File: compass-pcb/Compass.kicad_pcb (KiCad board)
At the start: 2 copper layers, 6 parts

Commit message: adding comments to psb
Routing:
- net (no net): track 950.9 -> 913.0 mm, vias 36 -> 38
- net GND: track 142.4 -> 175.8 mm, vias 6 -> 8
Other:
- board text added: "Battery"
- board text added: "Encoder"
- board text added: "GPS"
- board text added: "Hall Sensor (B)"
- board text added: "Power (charge/ discharge)"
- board text added: "Servo (A)"

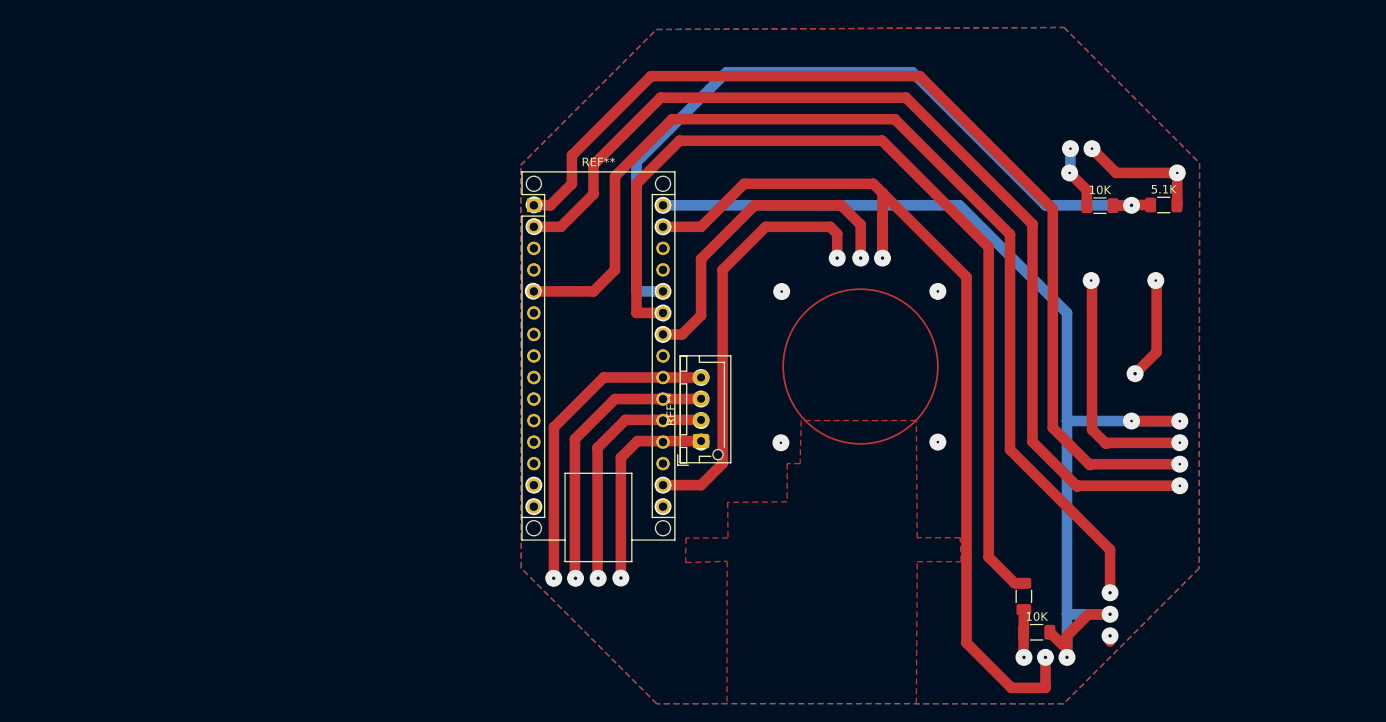
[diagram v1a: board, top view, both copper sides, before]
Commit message: adding battery jumper
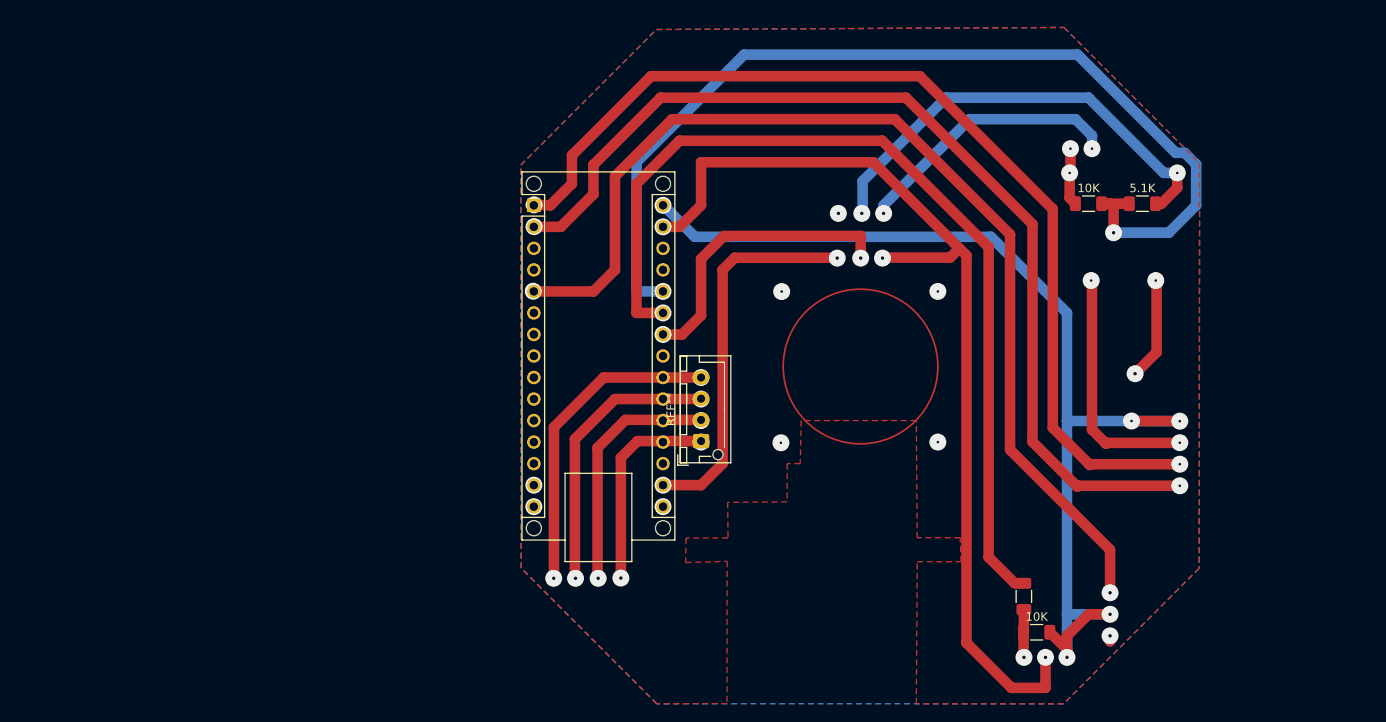
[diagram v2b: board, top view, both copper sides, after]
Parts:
- moved 5.1K 2.52 mm to (240.0, 76.0)
- moved 10K 1.36 mm to (233.7, 76.0)
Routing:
- net (no net): track 913.0 -> 1000.3 mm, vias 38 -> 41
- net GND: track 175.8 -> 179.2 mm
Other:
- board text added: "Battery gnd +"
- board text added: "Battery jumper"
- board text removed: "Battery"

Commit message: playing with placing main switch on the board
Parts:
- added  : , Connector_Wire:SolderWire-0.5sqmm_1x01_D0.9mm_OD2.1mm, F.Cu at (209.5, 82.4)
- added REF**: SolderWire-1.5sqmm_1x01_D1.7mm_OD3.9mm, Connector_Wire:SolderWire-1.5sqmm_1x01_D1.7mm_OD3.9mm, F.Cu at (264.2, 91.4)
- added REF**: SolderWire-2.5sqmm_1x01_D2.4mm_OD3.6mm, Connector_Wire:SolderWire-2.5sqmm_1x01_D2.4mm_OD3.6mm, F.Cu at (264.2, 83.8)
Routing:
- net (no net): track 1000.3 -> 1003.8 mm, vias 41 -> 58
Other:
- board text added: "on/off slide switch"

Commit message: Revert "playing with placing main switch on the board"
This reverts commit f90624a9c38ec8366b61e906c035f362712ec212.
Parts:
- removed  : , Connector_Wire:SolderWire-0.5sqmm_1x01_D0.9mm_OD2.1mm
- removed the REF** at (264.2, 91.4)
- removed the REF** at (264.2, 83.8)
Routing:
- net (no net): track 1003.8 -> 1000.3 mm, vias 58 -> 41
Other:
- board text removed: "on/off slide switch"

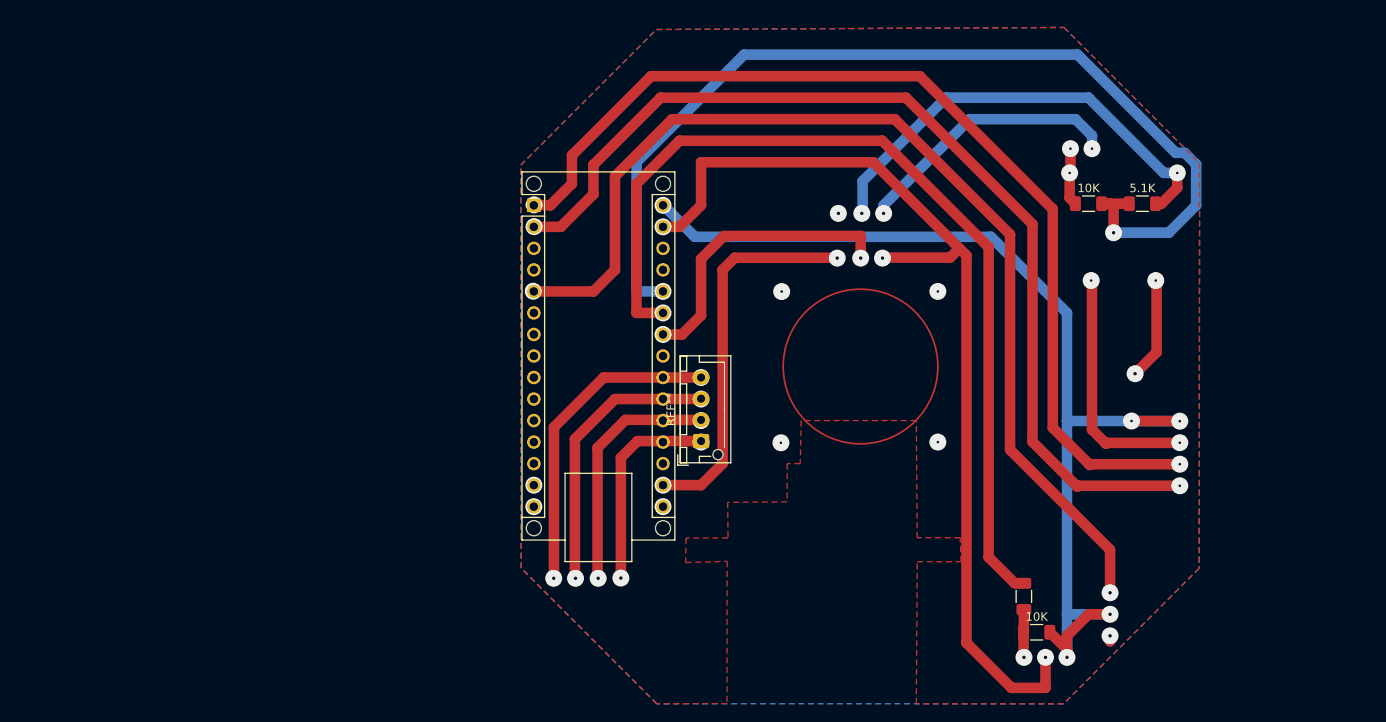
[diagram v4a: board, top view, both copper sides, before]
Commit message: Update Compass.kicad_pcb
moving battery jumper
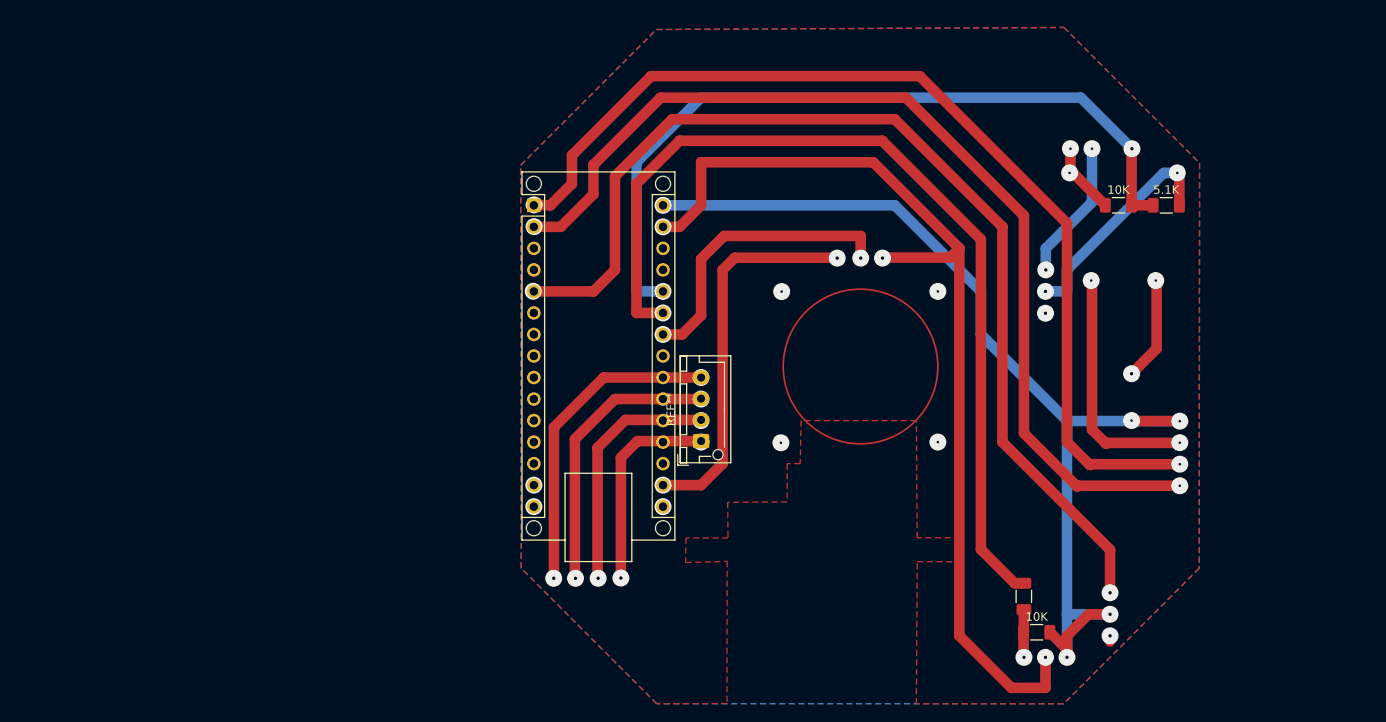
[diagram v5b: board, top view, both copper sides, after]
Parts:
- moved 10K 3.54 mm to (237.2, 76.2)
- moved 5.1K 2.82 mm to (242.8, 76.2)
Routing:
- net (no net): track 1000.3 -> 929.3 mm

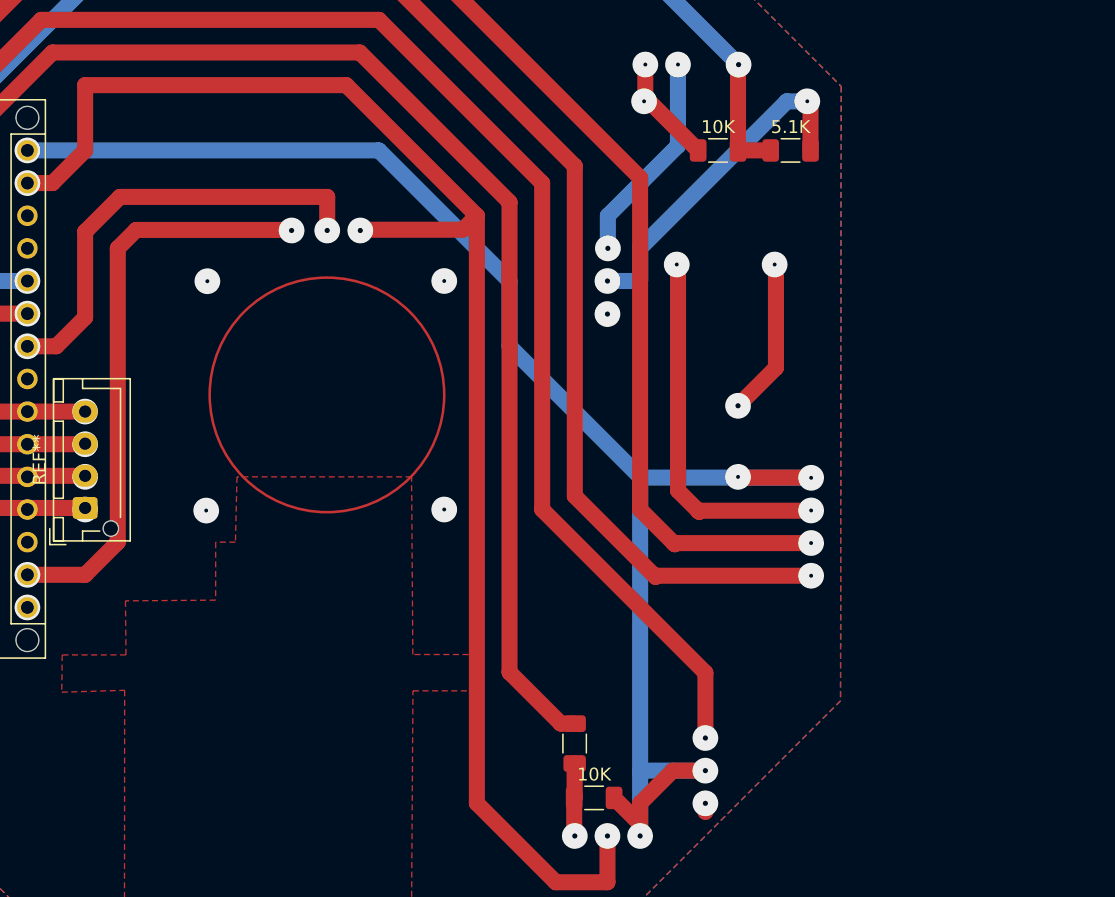
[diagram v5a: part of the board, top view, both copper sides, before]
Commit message: adding spacing for ground connectors
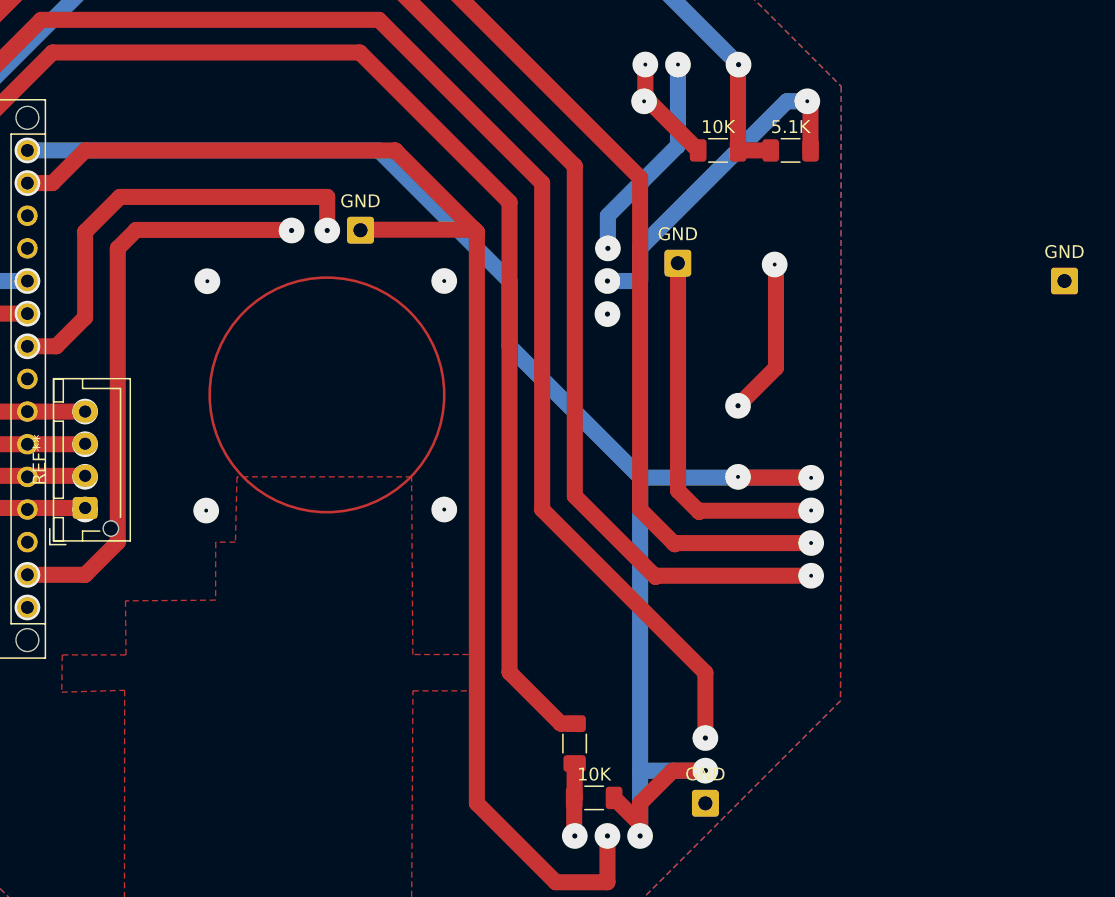
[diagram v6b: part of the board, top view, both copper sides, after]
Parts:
- added GND: , Connector_Wire:SolderWire-0.5sqmm_1x01_D0.9mm_OD2.1mm, F.Cu at (264.2, 86.4)
- added GND: , Connector_Wire:SolderWire-0.5sqmm_1x01_D0.9mm_OD2.1mm, F.Cu at (234.1, 85.0)
- added GND: , Connector_Wire:SolderWire-0.5sqmm_1x01_D0.9mm_OD2.1mm, F.Cu at (209.4, 82.4)
- added GND: , Connector_Wire:SolderWire-0.5sqmm_1x01_D0.9mm_OD2.1mm, F.Cu at (236.2, 127.0)
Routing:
- net GND: track 179.2 -> 171.1 mm, vias 8 -> 5
